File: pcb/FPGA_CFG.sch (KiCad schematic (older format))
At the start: 5 parts, among them U4 iCE40-HX8K-CT256, U6 SPI Flash

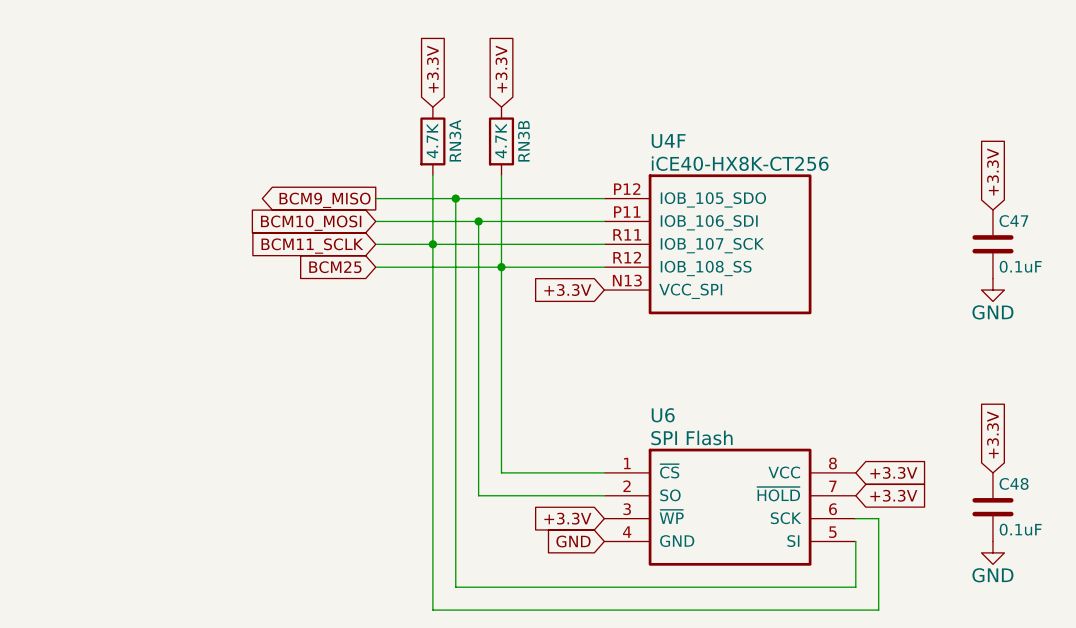
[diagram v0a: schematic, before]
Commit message: Added series resistors between RPi connector and FPGA/flash SPI pins. * Increased voltage/ground zone clearances from 6mil to 10mil. * Placed VCCIO_3 voltage / R8 resistor table in bottom silkscreen.
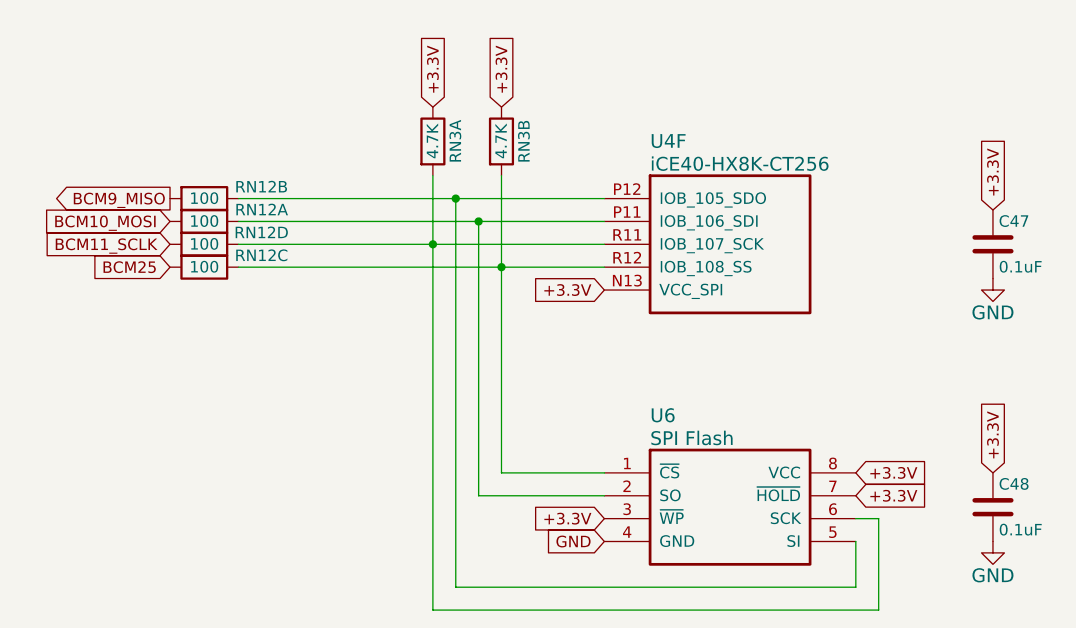
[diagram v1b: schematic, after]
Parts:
- added RN12: 100, XESS:CTS_742C083, symbol RN4
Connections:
- net BCM10_MOSI: now also RN12.1; no longer U4.P11 (IOB_106_SDI), U6.2 (SO)
- net BCM11_SCLK: now also RN12.4; no longer RN3.1, U4.R11 (IOB_107_SCK), U6.6 (SCK)
- net BCM25: now also RN12.3; no longer RN3.2, U4.R12 (IOB_108_SS), U6.1 (~CS)
- net BCM9_MISO: now also RN12.2; no longer U4.P12 (IOB_105_SDO), U6.5 (SI)
- new net: RN12.8, U4.P11 (IOB_106_SDI), U6.2 (SO)
- new net: RN12.7, U4.P12 (IOB_105_SDO), U6.5 (SI)
- new net: RN12.5, RN3.1, U4.R11 (IOB_107_SCK), U6.6 (SCK)
- new net: RN12.6, RN3.2, U4.R12 (IOB_108_SS), U6.1 (~CS)
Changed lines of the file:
@@
 Sheet 5 7
 Title "CAT HAT"
-Date "2015-09-09"
-Rev "0.1"
+Date "2016-03-14"
+Rev "0.2"
 Comp "XESS Corp."
-Comment1 "(c) 2015"
+Comment1 "(c) 2015 - 2016"
 Comment2 "OSHW"
 Comment3 "CC BY 4.0"
@@
 +3.3V
 Wire Wire Line
-	4600 3600 5600 3600
+	4000 3600 5600 3600
 Wire Wire Line
 	4950 5200 6700 5200
@@
 	6700 5200 6700 5000
 Wire Wire Line
-	4600 3500 5600 3500
+	4000 3500 5600 3500
 Wire Wire Line
 	5050 4800 5600 4800
 Wire Wire Line
-	4600 3700 5600 3700
+	4000 3700 5600 3700
 Wire Wire Line
 	4850 3400 4850 5300
@@
 Connection ~ 4850 3700
 Wire Wire Line
-	4600 3800 5600 3800
+	4000 3800 5600 3800
 Wire Wire Line
 	5150 3400 5150 4700
@@
 	5150 4700 5600 4700
 Connection ~ 5150 3800
-Text GLabel 4600 3700 0    50   Input ~ 0
+Text GLabel 3700 3700 0    50   Input ~ 0
 BCM11_SCLK
-Text GLabel 4600 3500 0    50   Output ~ 0
+Text GLabel 3700 3500 0    50   Output ~ 0
 BCM9_MISO
-Text GLabel 4600 3600 0    50   Input ~ 0
+Text GLabel 3700 3600 0    50   Input ~ 0
 BCM10_MOSI
 $Comp
@@
 	0    -1   -1   0
 $EndComp
-Text GLabel 4600 3800 0    50   Input ~ 0
+Text GLabel 3700 3800 0    50   Input ~ 0
 BCM25
 $Bitmap
@@
 	5050 4800 5050 3600
 Connection ~ 5050 3600
+$Comp
+L RN4 RN12
+U 1 1 56E77223
+P 3700 3600
+F 0 "RN12" H 4100 3650 50  0000 C CNN
+F 1 "100" H 3850 3600 50  0000 C CNN
+F 2 "XESS:CTS_742C083" H 3700 3600 50  0001 C CNN
+F 3 "" H 3700 3600 50  0000 C CNN
+	1    3700 3600
+	1    0    0    -1
+$EndComp
+$Comp
+L RN4 RN12
+U 2 1 56E7725F
+P 3700 3500
+F 0 "RN12" H 4100 3550 50  0000 C CNN
+F 1 "100" H 3850 3500 50  0000 C CNN
+F 2 "XESS:CTS_742C083" H 3700 3500 50  0001 C CNN
+F 3 "" H 3700 3500 50  0000 C CNN
+	2    3700 3500
+	1    0    0    -1
+$EndComp
+$Comp
+L RN4 RN12
+U 3 1 56E772A7
+P 3700 3800
+F 0 "RN12" H 4100 3850 50  0000 C CNN
+F 1 "100" H 3850 3800 50  0000 C CNN
+F 2 "XESS:CTS_742C083" H 3700 3800 50  0001 C CNN
+F 3 "" H 3700 3800 50  0000 C CNN
+	3    3700 3800
+	1    0    0    -1
+$EndComp
+$Comp
+L RN4 RN12
+U 4 1 56E772F7
+P 3700 3700
+F 0 "RN12" H 4100 3750 50  0000 C CNN
+F 1 "100" H 3850 3700 50  0000 C CNN
+F 2 "XESS:CTS_742C083" H 3700 3700 50  0001 C CNN
+F 3 "" H 3700 3700 50  0000 C CNN
+	4    3700 3700
+	1    0    0    -1
+$EndComp
 $EndSCHEMATC

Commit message: Added assembly order field to schematic.
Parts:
- C47: assembly_order (none) -> 25
- C48: assembly_order (none) -> 63
- RN12: assembly_order (none) -> 49
- RN3: assembly_order (none) -> 50
- U4: assembly_order (none) -> 1; manf# (none) -> ICE40HX8K-CT256
- U6: assembly_order (none) -> 74
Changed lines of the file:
@@
 U 6 1 55F04F56
 P 5600 3500
-AR Path="/55DF5F27/55E883EA/55F04F56" Ref="U?"  Part="6"
-AR Path="/55DF5F27/55E883EA/55F049E9/55F04F56" Ref="U4"  Part="6"
-AR Path="/55F04F56" Ref="U?"  Part="6"
-F 0 "U4" H 5800 3750 60  0000 L CNN
-F 1 "iCE40-HX8K-CT256" H 5800 3650 60  0000 L CNN
-F 2 "XESS:Lattice_caBGA_256" H 5600 3500 60  0001 C CNN
-F 3 "" H 5600 3500 60  0000 C CNN
+AR Path="/55DF5F27/55E883EA/55F04F56" Ref="U?" Part="6"
+AR Path="/55DF5F27/55E883EA/55F049E9/55F04F56" Ref="U4" Part="6"
+AR Path="/55F04F56" Ref="U?" Part="6"
+F 0 "U4" H 5800 3750 60 0000 L CNN
+F 1 "iCE40-HX8K-CT256" H 5800 3650 60 0000 L CNN
+F 2 "XESS:Lattice_caBGA_256" H 5600 3500 60 0001 C CNN
+F 3 "" H 5600 3500 60 0000 C CNN
+F 4 "1" H 0 0 50 0001 C CNN "assembly_order"
+F 5 "ICE40HX8K-CT256" H 0 0 50 0001 C CNN "manf#"
 	6    5600 3500
 	1    0    0    -1
 $EndComp
-Text GLabel 5600 3900 0    50   Input ~ 0
-+3.3V
 $Comp
 L SERIAL_FLASH U6
 U 1 1 55F04F6B
 P 5600 4700
-F 0 "U6" H 5800 4950 60  0000 L CNN
-F 1 "SPI Flash" H 5800 4850 60  0000 L CNN
-F 2 "SMD_Packages:SOIC-8-N" H 5600 4700 50  0001 C CNN
-F 3 "" H 5600 4700 50  0000 C CNN
-F 4 "AT25SF041-SSHD-T" H 5600 4700 60  0001 C CNN "manf#"
+F 0 "U6" H 5800 4950 60 0000 L CNN
+F 1 "SPI Flash" H 5800 4850 60 0000 L CNN
+F 2 "SMD_Packages:SOIC-8-N" H 5600 4700 50 0001 C CNN
+F 3 "" H 5600 4700 50 0000 C CNN
+F 4 "74" H 0 0 50 0001 C CNN "assembly_order"
+F 5 "AT25SF041-SSHD-T" H 5600 4700 60 0001 C CNN "manf#"
 	1    5600 4700
 	1    0    0    -1
 $EndComp
-Text GLabel 6700 4700 2    50   Input ~ 0
-+3.3V
-Text GLabel 5600 5000 0    50   Input ~ 0
-GND
-Text GLabel 6700 4800 2    50   Input ~ 0
-+3.3V
-Text GLabel 5600 4900 0    50   Input ~ 0
-+3.3V
-Text GLabel 5150 3100 1    50   Input ~ 0
-+3.3V
-Text GLabel 7300 3550 1    50   Input ~ 0
-+3.3V
 $Comp
 L C C47
 U 1 1 55F05A0B
 P 7300 3700
-F 0 "C47" H 7325 3800 50  0000 L CNN
-F 1 "0.1uF" H 7325 3600 50  0000 L CNN
-F 2 "Capacitors_SMD:C_0603" H 7338 3550 30  0001 C CNN
-F 3 "" H 7300 3700 60  0000 C CNN
+F 0 "C47" H 7325 3800 50 0000 L CNN
+F 1 "0.1uF" H 7325 3600 50 0000 L CNN
+F 2 "Capacitors_SMD:C_0603" H 7338 3550 30 0001 C CNN
+F 3 "" H 7300 3700 60 0000 C CNN
+F 4 "25" H 0 0 50 0001 C CNN "assembly_order"
 	1    7300 3700
 	1    0    0    -1
 $EndComp
 $Comp
-L GND #PWR051
-U 1 1 55F05A12
-P 7300 3850
-F 0 "#PWR051" H 7300 3600 60  0001 C CNN
-F 1 "GND" H 7300 3700 60  0000 C CNN
-F 2 "" H 7300 3850 60  0000 C CNN
-F 3 "" H 7300 3850 60  0000 C CNN
-	1    7300 3850
-	1    0    0    -1
-$EndComp
-Text GLabel 7300 4700 1    50   Input ~ 0
-+3.3V
-$Comp
 L C C48
 U 1 1 55F05BFC
 P 7300 4850
-F 0 "C48" H 7325 4950 50  0000 L CNN
-F 1 "0.1uF" H 7325 4750 50  0000 L CNN
-F 2 "Capacitors_SMD:C_0603" H 7338 4700 30  0001 C CNN
-F 3 "" H 7300 4850 60  0000 C CNN
+F 0 "C48" H 7325 4950 50 0000 L CNN
+F 1 "0.1uF" H 7325 4750 50 0000 L CNN
+F 2 "Capacitors_SMD:C_0603" H 7338 4700 30 0001 C CNN
+F 3 "" H 7300 4850 60 0000 C CNN
+F 4 "63" H 0 0 50 0001 C CNN "assembly_order"
 	1    7300 4850
 	1    0    0    -1
 $EndComp
 $Comp
-L GND #PWR052
+L GND #PWR053
 U 1 1 55F05C02
 P 7300 5000
-F 0 "#PWR052" H 7300 4750 60  0001 C CNN
-F 1 "GND" H 7300 4850 60  0000 C CNN
-F 2 "" H 7300 5000 60  0000 C CNN
-F 3 "" H 7300 5000 60  0000 C CNN
+F 0 "#PWR053" H 7300 4750 60 0001 C CNN
+F 1 "GND" H 7300 4850 60 0000 C CNN
+F 2 "" H 7300 5000 60 0000 C CNN
+F 3 "" H 7300 5000 60 0000 C CNN
 	1    7300 5000
 	1    0    0    -1
 $EndComp
-Text GLabel 4850 3100 1    50   Input ~ 0
-+3.3V
-Wire Wire Line
-	4000 3600 5600 3600
-Wire Wire Line
-	4950 5200 6700 5200
-Wire Wire Line
-	6700 5200 6700 5000
-Wire Wire Line
-	4000 3500 5600 3500
-Wire Wire Line
-	5050 4800 5600 4800
-Wire Wire Line
-	4000 3700 5600 3700
-Wire Wire Line
-	4850 3400 4850 5300
-Wire Wire Line
-	4850 5300 6800 5300
-Wire Wire Line
-	6800 5300 6800 4900
-Wire Wire Line
-	6800 4900 6700 4900
-Connection ~ 4850 3700
-Wire Wire Line
-	4000 3800 5600 3800
-Wire Wire Line
-	5150 3400 5150 4700
-Wire Wire Line
-	5150 4700 5600 4700
-Connection ~ 5150 3800
-Text GLabel 3700 3700 0    50   Input ~ 0
-BCM11_SCLK
-Text GLabel 3700 3500 0    50   Output ~ 0
-BCM9_MISO
-Text GLabel 3700 3600 0    50   Input ~ 0
-BCM10_MOSI
 $Comp
 L RN2 RN3
 U 1 1 55F0D803
 P 4850 3400
-F 0 "RN3" H 5000 3300 50  0000 C CNN
-F 1 "4.7K" H 5000 3400 50  0000 C CNN
-F 2 "XESS:CTS_742C043" H 4850 3400 50  0001 C CNN
-F 3 "" H 4850 3400 50  0000 C CNN
+F 0 "RN3" H 5000 3300 50 0000 C CNN
+F 1 "4.7K" H 5000 3400 50 0000 C CNN
+F 2 "XESS:CTS_742C043" H 4850 3400 50 0001 C CNN
+F 3 "" H 4850 3400 50 0000 C CNN
+F 4 "50" H 0 0 50 0001 C CNN "assembly_order"
 	1    4850 3400
 	0    -1   -1   0
@@
 U 2 1 55F0D8A0
 P 5150 3400
-F 0 "RN3" H 5300 3300 50  0000 C CNN
-F 1 "4.7K" H 5300 3400 50  0000 C CNN
-F 2 "XESS:CTS_742C043" H 5150 3400 50  0001 C CNN
-F 3 "" H 5150 3400 50  0000 C CNN
+F 0 "RN3" H 5300 3300 50 0000 C CNN
+F 1 "4.7K" H 5300 3400 50 0000 C CNN
+F 2 "XESS:CTS_742C043" H 5150 3400 50 0001 C CNN
+F 3 "" H 5150 3400 50 0000 C CNN
+F 4 "50" H 0 0 50 0001 C CNN "assembly_order"
 	2    5150 3400
 	0    -1   -1   0
 $EndComp
-Text GLabel 3700 3800 0    50   Input ~ 0
-BCM25
+$Comp
+L RN4 RN12
+U 1 1 56E77223
+P 3700 3600
+F 0 "RN12" H 4100 3650 50 0000 C CNN
+F 1 "100" H 3850 3600 50 0000 C CNN
+F 2 "XESS:CTS_742C083" H 3700 3600 50 0001 C CNN
+F 3 "" H 3700 3600 50 0000 C CNN
+F 4 "49" H 0 0 50 0001 C CNN "assembly_order"
+	1    3700 3600
+	1    0    0    -1
+$EndComp
+$Comp
+L RN4 RN12
+U 2 1 56E7725F
+P 3700 3500
+F 0 "RN12" H 4100 3550 50 0000 C CNN
+F 1 "100" H 3850 3500 50 0000 C CNN
+F 2 "XESS:CTS_742C083" H 3700 3500 50 0001 C CNN
+F 3 "" H 3700 3500 50 0000 C CNN
+F 4 "49" H 0 0 50 0001 C CNN "assembly_order"
+	2    3700 3500
+	1    0    0    -1
+$EndComp
+$Comp
+L RN4 RN12
+U 3 1 56E772A7
+P 3700 3800
+F 0 "RN12" H 4100 3850 50 0000 C CNN
+F 1 "100" H 3850 3800 50 0000 C CNN
+F 2 "XESS:CTS_742C083" H 3700 3800 50 0001 C CNN
+F 3 "" H 3700 3800 50 0000 C CNN
+F 4 "49" H 0 0 50 0001 C CNN "assembly_order"
+	3    3700 3800
+	1    0    0    -1
+$EndComp
+$Comp
+L RN4 RN12
+U 4 1 56E772F7
+P 3700 3700
+F 0 "RN12" H 4100 3750 50 0000 C CNN
+F 1 "100" H 3850 3700 50 0000 C CNN
+F 2 "XESS:CTS_742C083" H 3700 3700 50 0001 C CNN
+F 3 "" H 3700 3700 50 0000 C CNN
+F 4 "49" H 0 0 50 0001 C CNN "assembly_order"
+	4    3700 3700
+	1    0    0    -1
+$EndComp
+$Comp
+L GND #PWR054
+U 1 1 56EB84D3
+P 7300 3850
+F 0 "#PWR054" H 7300 3600 60 0001 C CNN
+F 1 "GND" H 7300 3700 60 0000 C CNN
+F 2 "" H 7300 3850 60 0000 C CNN
+F 3 "" H 7300 3850 60 0000 C CNN
+	1    7300 3850
+	1    0    0    -1
+$EndComp
 $Bitmap
 Pos 9850 6850
@@
 55 BA E9 1E 45 C1 A5 AE 83 10 42 08 21 84 10 62 29 92 A4 84 10 42 08 21 84 10 C2 A9 94 F3 E7 B9
 8E 61 2D AC 28 7C D0 75 10 42 08 21 84 10 42 2C 45 FF 1F 5C 99 D7 EB 78 7F 83 BD 00 00 00 00 49
-45 4E 44 AE 42 60 82 00
+45 4E 44 AE 42 60 82 3A
 EndData
 $EndBitmap
@@
 1E 25 49 2A DA F6 C4 5C B7 0C C3 B9 A4 0A 98 09 FC 0D B0 92 CD 57 CD 1F 06 4E 04 26 A7 75 27 49
 52 39 26 13 73 DE C3 6C BE 70 B5 12 F8 16 86 73 8D C3 FF 03 63 F8 EE 2E BE 9A 04 B1 00 00 00 00
-49 45 4E 44 AE 42 60 82 5D
+49 45 4E 44 AE 42 60 82 AE
 EndData
 $EndBitmap
+Text GLabel 5600 3900 0    50   Input ~ 0
++3.3V
+Text GLabel 6700 4700 2    50   Input ~ 0
++3.3V
+Text GLabel 5600 5000 0    50   Input ~ 0
+GND
+Text GLabel 6700 4800 2    50   Input ~ 0
++3.3V
+Text GLabel 5600 4900 0    50   Input ~ 0
++3.3V
+Text GLabel 5150 3100 1    50   Input ~ 0
++3.3V
+Text GLabel 7300 3550 1    50   Input ~ 0
++3.3V
+Text GLabel 7300 4700 1    50   Input ~ 0
++3.3V
+Text GLabel 4850 3100 1    50   Input ~ 0
++3.3V
+Text GLabel 3700 3700 0    50   Input ~ 0
+BCM11_SCLK
+Text GLabel 3700 3500 0    50   Output ~ 0
+BCM9_MISO
+Text GLabel 3700 3600 0    50   Input ~ 0
+BCM10_MOSI
+Text GLabel 3700 3800 0    50   Input ~ 0
+BCM25
+Wire Wire Line
+	4000 3600 5600 3600
+Wire Wire Line
+	4950 5200 6700 5200
+Wire Wire Line
+	6700 5200 6700 5000
+Wire Wire Line
+	4000 3500 5600 3500
+Wire Wire Line
+	5050 4800 5600 4800
+Wire Wire Line
+	4000 3700 5600 3700
+Wire Wire Line
+	4850 3400 4850 5300
+Wire Wire Line
+	4850 5300 6800 5300
+Wire Wire Line
+	6800 5300 6800 4900
+Wire Wire Line
+	6800 4900 6700 4900
+Wire Wire Line
+	4000 3800 5600 3800
+Wire Wire Line
+	5150 3400 5150 4700
+Wire Wire Line
+	5150 4700 5600 4700
 Wire Wire Line
 	4950 5200 4950 3500
-Connection ~ 4950 3500
 Wire Wire Line
 	5050 4800 5050 3600
+Connection ~ 4850 3700
+Connection ~ 5150 3800
+Connection ~ 4950 3500
 Connection ~ 5050 3600
-$Comp
-L RN4 RN12
-U 1 1 56E77223
-P 3700 3600
-F 0 "RN12" H 4100 3650 50  0000 C CNN
-F 1 "100" H 3850 3600 50  0000 C CNN
-F 2 "XESS:CTS_742C083" H 3700 3600 50  0001 C CNN
-F 3 "" H 3700 3600 50  0000 C CNN
-	1    3700 3600
-	1    0    0    -1
-$EndComp
-$Comp
-L RN4 RN12
-U 2 1 56E7725F
-P 3700 3500
-F 0 "RN12" H 4100 3550 50  0000 C CNN
-F 1 "100" H 3850 3500 50  0000 C CNN
-F 2 "XESS:CTS_742C083" H 3700 3500 50  0001 C CNN
-F 3 "" H 3700 3500 50  0000 C CNN
-	2    3700 3500
-	1    0    0    -1
-$EndComp
-$Comp
-L RN4 RN12
-U 3 1 56E772A7
-P 3700 3800
-F 0 "RN12" H 4100 3850 50  0000 C CNN
-F 1 "100" H 3850 3800 50  0000 C CNN
-F 2 "XESS:CTS_742C083" H 3700 3800 50  0001 C CNN
-F 3 "" H 3700 3800 50  0000 C CNN
-	3    3700 3800
-	1    0    0    -1
-$EndComp
-$Comp
-L RN4 RN12
-U 4 1 56E772F7
-P 3700 3700
-F 0 "RN12" H 4100 3750 50  0000 C CNN
-F 1 "100" H 3850 3700 50  0000 C CNN
-F 2 "XESS:CTS_742C083" H 3700 3700 50  0001 C CNN
-F 3 "" H 3700 3700 50  0000 C CNN
-	4    3700 3700
-	1    0    0    -1
-$EndComp
 $EndSCHEMATC

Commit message: Assembly order field stopped propagation of part numbers, so I added them to each part using kifield.
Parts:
- C47, C48: manf# (none) -> GRM188R71C104KA01D
- RN12: manf# (none) -> 741C083101JP
- RN3: manf# (none) -> 742C043472JP
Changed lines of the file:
@@
 F 3 "" H 7300 3700 60 0000 C CNN
 F 4 "25" H 0 0 50 0001 C CNN "assembly_order"
+F 5 "GRM188R71C104KA01D" H 0 0 50 0001 C CNN "manf#"
 	1    7300 3700
 	1    0    0    -1
@@
 F 3 "" H 7300 4850 60 0000 C CNN
 F 4 "63" H 0 0 50 0001 C CNN "assembly_order"
+F 5 "GRM188R71C104KA01D" H 0 0 50 0001 C CNN "manf#"
 	1    7300 4850
 	1    0    0    -1
@@
 F 3 "" H 4850 3400 50 0000 C CNN
 F 4 "50" H 0 0 50 0001 C CNN "assembly_order"
+F 5 "742C043472JP" H 0 0 50 0001 C CNN "manf#"
 	1    4850 3400
 	0    -1   -1   0
@@
 F 3 "" H 5150 3400 50 0000 C CNN
 F 4 "50" H 0 0 50 0001 C CNN "assembly_order"
+F 5 "742C043472JP" H 0 0 50 0001 C CNN "manf#"
 	2    5150 3400
 	0    -1   -1   0
@@
 F 3 "" H 3700 3600 50 0000 C CNN
 F 4 "49" H 0 0 50 0001 C CNN "assembly_order"
+F 5 "741C083101JP" H 0 0 50 0001 C CNN "manf#"
 	1    3700 3600
 	1    0    0    -1
@@
 F 3 "" H 3700 3500 50 0000 C CNN
 F 4 "49" H 0 0 50 0001 C CNN "assembly_order"
+F 5 "741C083101JP" H 0 0 50 0001 C CNN "manf#"
 	2    3700 3500
 	1    0    0    -1
@@
 F 3 "" H 3700 3800 50 0000 C CNN
 F 4 "49" H 0 0 50 0001 C CNN "assembly_order"
+F 5 "741C083101JP" H 0 0 50 0001 C CNN "manf#"
 	3    3700 3800
 	1    0    0    -1
@@
 F 3 "" H 3700 3700 50 0000 C CNN
 F 4 "49" H 0 0 50 0001 C CNN "assembly_order"
+F 5 "741C083101JP" H 0 0 50 0001 C CNN "manf#"
 	4    3700 3700
 	1    0    0    -1

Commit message: Works with KiCad V5.
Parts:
- C47, C48: symbol C -> device:C
- RN12: symbol RN4 -> XESS:RN4
- RN3: symbol RN2 -> XESS:RN2
- U4: symbol iCE40-HX8K-CT256 -> Lattice-iCE:iCE40-HX8K-CT256
- U6: symbol SERIAL_FLASH -> CAT-rescue:SERIAL_FLASH
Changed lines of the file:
@@
-EESchema Schematic File Version 2
-LIBS:CAT-rescue
-LIBS:power
-LIBS:device
-LIBS:transistors
-LIBS:conn
-LIBS:linear
-LIBS:regul
-LIBS:74xx
-LIBS:cmos4000
-LIBS:adc-dac
-LIBS:memory
-LIBS:xilinx
-LIBS:microcontrollers
-LIBS:dsp
-LIBS:microchip
-LIBS:analog_switches
-LIBS:motorola
-LIBS:texas
-LIBS:intel
-LIBS:audio
-LIBS:interface
-LIBS:digital-audio
-LIBS:philips
-LIBS:display
-LIBS:cypress
-LIBS:siliconi
-LIBS:opto
-LIBS:atmel
-LIBS:contrib
-LIBS:valves
-LIBS:xess
-LIBS:Cypress_PSoC
-LIBS:Cypress_cy8c5xlp
-LIBS:Lattice_iCE_FPGA
-LIBS:xilinx7
-LIBS:xilinx6v
-LIBS:xilinx6s
-LIBS:xula
-LIBS:espressif-xess
+EESchema Schematic File Version 4
 LIBS:CAT-cache
 EELAYER 26 0
@@
 $EndDescr
 $Comp
-L iCE40-HX8K-CT256 U?
+L Lattice-iCE:iCE40-HX8K-CT256 U?
 U 6 1 55F04F56
 P 5600 3500
@@
 $EndComp
 $Comp
-L SERIAL_FLASH U6
+L CAT-rescue:SERIAL_FLASH U6
 U 1 1 55F04F6B
 P 5600 4700
@@
 $EndComp
 $Comp
-L C C47
+L device:C C47
 U 1 1 55F05A0B
 P 7300 3700
@@
 $EndComp
 $Comp
-L C C48
+L device:C C48
 U 1 1 55F05BFC
 P 7300 4850
@@
 $EndComp
 $Comp
-L GND #PWR053
+L power1:GND #PWR053
 U 1 1 55F05C02
 P 7300 5000
@@
 $EndComp
 $Comp
-L RN2 RN3
+L XESS:RN2 RN3
 U 1 1 55F0D803
 P 4850 3400
@@
 $EndComp
 $Comp
-L RN2 RN3
+L XESS:RN2 RN3
 U 2 1 55F0D8A0
 P 5150 3400
@@
 $EndComp
 $Comp
-L RN4 RN12
+L XESS:RN4 RN12
 U 1 1 56E77223
 P 3700 3600
@@
 $EndComp
 $Comp
-L RN4 RN12
+L XESS:RN4 RN12
 U 2 1 56E7725F
 P 3700 3500
@@
 $EndComp
 $Comp
-L RN4 RN12
+L XESS:RN4 RN12
 U 3 1 56E772A7
 P 3700 3800
@@
 $EndComp
 $Comp
-L RN4 RN12
+L XESS:RN4 RN12
 U 4 1 56E772F7
 P 3700 3700
@@
 $EndComp
 $Comp
-L GND #PWR054
+L power1:GND #PWR054
 U 1 1 56EB84D3
 P 7300 3850
@@
 BCM25
 Wire Wire Line
-	4000 3600 5600 3600
+	4000 3600 5050 3600
 Wire Wire Line
 	4950 5200 6700 5200
@@
 	6700 5200 6700 5000
 Wire Wire Line
-	4000 3500 5600 3500
+	4000 3500 4950 3500
 Wire Wire Line
 	5050 4800 5600 4800
 Wire Wire Line
-	4000 3700 5600 3700
+	4000 3700 4850 3700
 Wire Wire Line
-	4850 3400 4850 5300
+	4850 3400 4850 3700
 Wire Wire Line
 	4850 5300 6800 5300
@@
 	6800 4900 6700 4900
 Wire Wire Line
-	4000 3800 5600 3800
+	4000 3800 5150 3800
 Wire Wire Line
-	5150 3400 5150 4700
+	5150 3400 5150 3800
 Wire Wire Line
 	5150 4700 5600 4700
@@
 Connection ~ 4950 3500
 Connection ~ 5050 3600
+Wire Wire Line
+	4850 3700 5600 3700
+Wire Wire Line
+	4850 3700 4850 5300
+Wire Wire Line
+	5150 3800 5600 3800
+Wire Wire Line
+	5150 3800 5150 4700
+Wire Wire Line
+	4950 3500 5600 3500
+Wire Wire Line
+	5050 3600 5600 3600
 $EndSCHEMATC
